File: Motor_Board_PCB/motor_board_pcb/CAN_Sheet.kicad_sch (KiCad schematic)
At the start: 13 parts, among them U1 MCP2515-xST, U2 TJA1050, Y1 20M

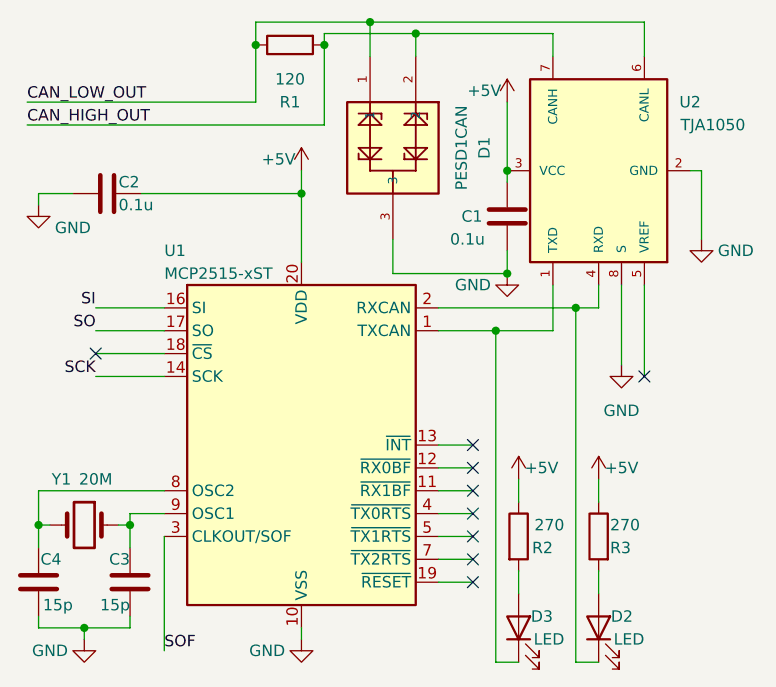
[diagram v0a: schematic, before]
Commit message: Integrated MCU to Motor board
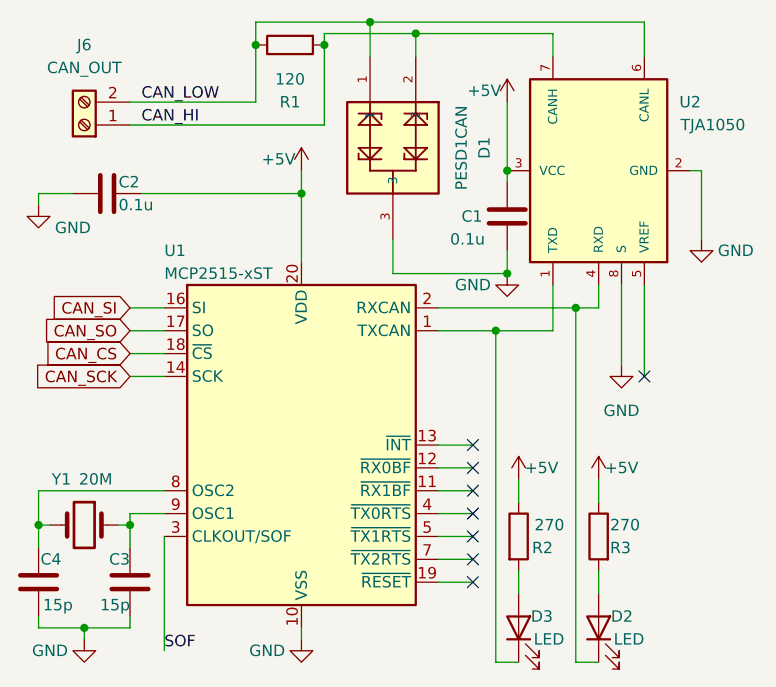
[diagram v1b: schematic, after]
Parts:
- added J6: CAN_OUT, symbol Connector:Screw_Terminal_01x02
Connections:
- net CAN_CS: now reaches U1.18 (~{CS})
- net CAN_HIGH_OUT renamed CAN_HI
- net CAN_HI: now also J6.1 (Pin_1)
- net CAN_LOW_OUT renamed CAN_LOW
- net CAN_LOW: now also J6.2 (Pin_2)
- net SCK renamed CAN_SCK
- net SI renamed CAN_SI
- net SO renamed CAN_SO
- no-connect marks 9 -> 8
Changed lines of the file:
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@@
   (junction (at 46.99 22.86) (diameter 0) (color 0 0 0 0)
   )
-  (no_connect (at 29.21 57.15))
   (no_connect (at 71.12 74.93))
   (no_connect (at 71.12 69.85))
@@
   (no_connect (at 71.12 77.47))
   (no_connect (at 71.12 82.55))
-  (wire (pts (xy 54.61 31.75) (xy 21.59 31.75))
+  (wire (pts (xy 54.61 31.75) (xy 33.02 31.75))
     (stroke (width 0) (type default))
   )
@@
     (stroke (width 0) (type default))
   )
-  (wire (pts (xy 29.21 52.07) (xy 36.83 52.07))
+  (wire (pts (xy 33.02 52.07) (xy 36.83 52.07))
     (stroke (width 0) (type default))
   )
@@
     (stroke (width 0) (type default))
   )
-  (wire (pts (xy 29.21 54.61) (xy 36.83 54.61))
+  (wire (pts (xy 33.02 54.61) (xy 36.83 54.61))
     (stroke (width 0) (type default))
   )
@@
     (stroke (width 0) (type default))
   )
-  (wire (pts (xy 29.21 57.15) (xy 36.83 57.15))
+  (wire (pts (xy 33.02 57.15) (xy 36.83 57.15))
     (stroke (width 0) (type default))
   )
@@
     (stroke (width 0) (type default))
   )
-  (wire (pts (xy 29.21 59.69) (xy 36.83 59.69))
+  (wire (pts (xy 33.02 59.69) (xy 36.83 59.69))
     (stroke (width 0) (type default))
   )
@@
     (stroke (width 0) (type default))
   )
-  (wire (pts (xy 21.59 29.21) (xy 46.99 29.21))
-    (stroke (width 0) (type default))
-  )
-  (label "CAN_HIGH_OUT" (at 21.59 31.75 0) (fields_autoplaced)
+  (wire (pts (xy 33.02 29.21) (xy 46.99 29.21))
+    (stroke (width 0) (type default))
+  )
+  (label "CAN_HI" (at 34.29 31.75 0) (fields_autoplaced)
     (effects (font (size 1.27 1.27)) (justify left bottom))
-  )
-  (label "SCK" (at 29.21 59.69 180) (fields_autoplaced)
-    (effects (font (size 1.27 1.27)) (justify right bottom))
   )
   (label "SOF" (at 36.83 90.17 0) (fields_autoplaced)
     (effects (font (size 1.27 1.27)) (justify left bottom))
   )
-  (label "SI" (at 29.21 52.07 180) (fields_autoplaced)
-    (effects (font (size 1.27 1.27)) (justify right bottom))
-  )
-  (label "SO" (at 29.21 54.61 180) (fields_autoplaced)
-    (effects (font (size 1.27 1.27)) (justify right bottom))
-  )
-  (label "CAN_LOW_OUT" (at 21.59 29.21 0) (fields_autoplaced)
+  (label "CAN_LOW" (at 34.29 29.21 0) (fields_autoplaced)
     (effects (font (size 1.27 1.27)) (justify left bottom))
+  )
+  (global_label "CAN_SI" (shape input) (at 33.02 52.07 180) (fields_autoplaced)
+    (effects (font (size 1.27 1.27)) (justify right))
+    (property "Intersheetrefs" "${INTERSHEET_REFS}" (at 23.1502 52.07 0)
+      (effects (font (size 1.27 1.27)) (justify right) hide)
+    )
+  )
+  (global_label "CAN_SCK" (shape input) (at 33.02 59.69 180) (fields_autoplaced)
+    (effects (font (size 1.27 1.27)) (justify right))
+    (property "Intersheetrefs" "${INTERSHEET_REFS}" (at 20.9789 59.69 0)
+      (effects (font (size 1.27 1.27)) (justify right) hide)
+    )
+  )
+  (global_label "CAN_CS" (shape input) (at 33.02 57.15 180) (fields_autoplaced)
+    (effects (font (size 1.27 1.27)) (justify right))
+    (property "Intersheetrefs" "${INTERSHEET_REFS}" (at 22.4591 57.15 0)
+      (effects (font (size 1.27 1.27)) (justify right) hide)
+    )
+  )
+  (global_label "CAN_SO" (shape input) (at 33.02 54.61 180) (fields_autoplaced)
+    (effects (font (size 1.27 1.27)) (justify right))
+    (property "Intersheetrefs" "${INTERSHEET_REFS}" (at 22.3611 54.61 0)
+      (effects (font (size 1.27 1.27)) (justify right) hide)
+    )
   )
   (symbol (lib_id "power:+5V") (at 52.07 36.83 0) (unit 1)
@@
         )
       )
+    )
+  )
+  (symbol (lib_id "Connector:Screw_Terminal_01x02") (at 27.94 31.75 180) (unit 1)
+    (in_bom yes) (on_board yes) (dnp no) (fields_autoplaced)
+    (property "Reference" "J6" (at 27.94 22.86 0)
+      (effects (font (size 1.27 1.27)))
+    )
+    (property "Value" "CAN_OUT" (at 27.94 25.4 0)
+      (effects (font (size 1.27 1.27)))
+    )
+    (property "Footprint" "" (at 27.94 31.75 0)
+      (effects (font (size 1.27 1.27)) hide)
+    )
+    (property "Datasheet" "~" (at 27.94 31.75 0)
+      (effects (font (size 1.27 1.27)) hide)
+    )
+    (pin "1")
+    (pin "2")
+    (instances
+      (project "motor_board_pcb"
+        (path "/4ad82a24-c992-45c9-b523-12e12bcd6ced/63c66207-e5d4-4f6f-af8f-451675dc3930"
+          (reference "J6") (unit 1)
+        )
+      )
